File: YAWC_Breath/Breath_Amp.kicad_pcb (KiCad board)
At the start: 2 copper layers, 41 x 32 mm, 20 parts, among them P1 J_IO, P2 PressSens, U1 MCP6002, U2 MPX12DP

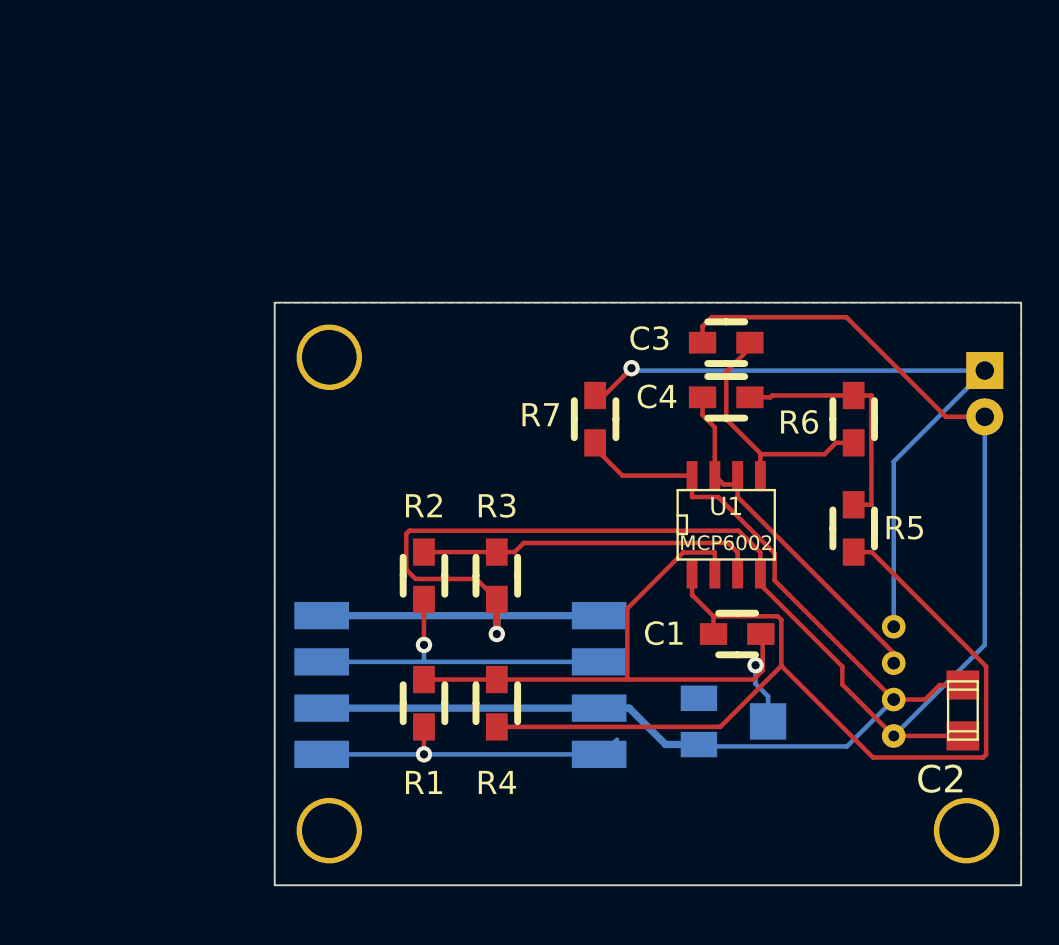
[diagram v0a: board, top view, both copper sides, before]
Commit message: Positioned connector and unrouted old
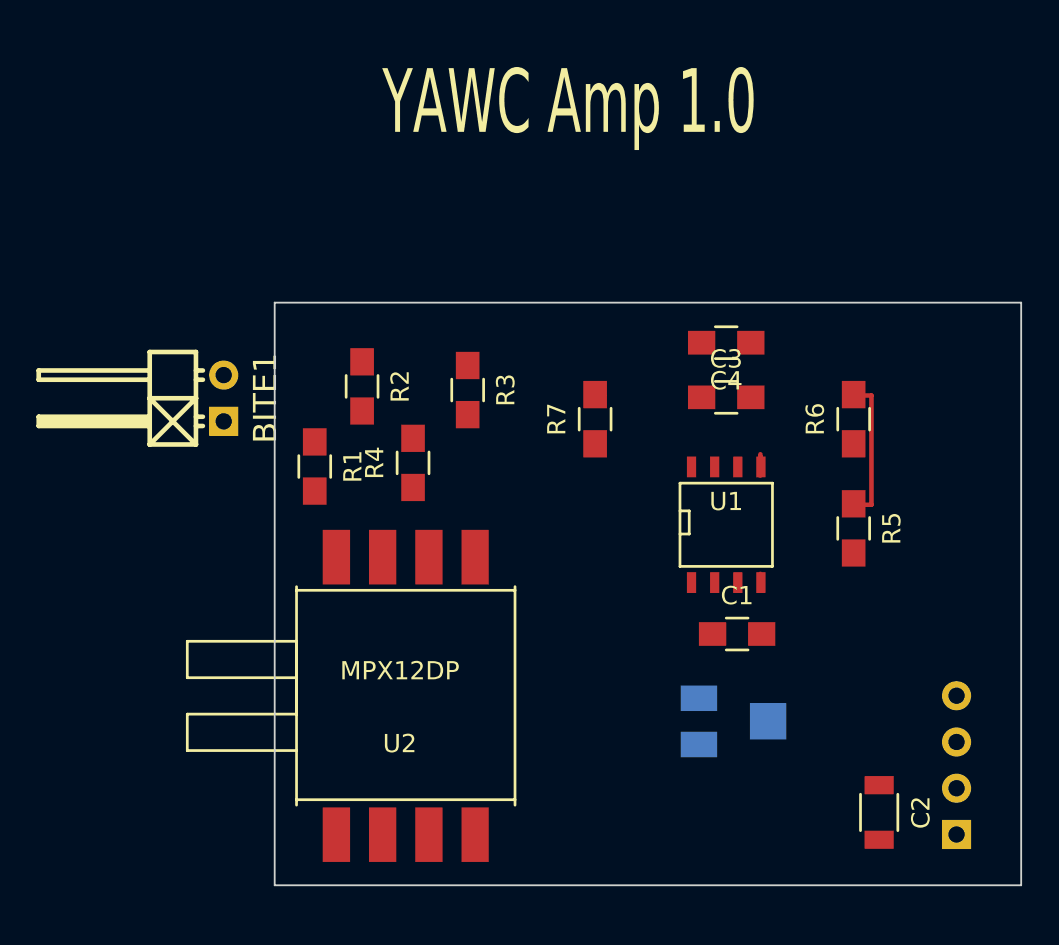
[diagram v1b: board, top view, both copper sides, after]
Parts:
- removed ?: , Wire_Pads:SolderWirePad_single_1-2mmDrill
- removed ? (x3): Hole, Mount:Hole3
- removed P2: PressSens, Pin_Headers:Pin_Header_Angled_1x02
- added BITE1: CONN_01X02, PIN_Hdr:Pin_Header_Angled_1x02, F.Cu at (141.0, 115.2)
- C1, C3, C4, R1, R2, R3, R4, R5, R6, R7: footprint Resistors_SMD:Resistor_SMD0805_HandSoldering -> Resistors_SMD:R_0805_HandSoldering
- C2: footprint Capacitors_SMD:c_1206 -> Capacitors_SMD:C_1206
- P1: footprint JST:JST-4-PH-RA -> PIN_Hdr:Pin_Header_Angled_1x04
- U1: footprint SOIC_Packages:SOIC-8_N -> SMD_Packages:SOIC-8-N
- U2: moved to F.Cu
- moved R1 14.3 mm to (146.0, 119.0)
- moved R4 14.0 mm to (151.4, 118.8)
- moved R2 10.9 mm to (148.6, 114.6)
- moved R3 10.3 mm to (154.4, 114.8)
- moved C2 7.25 mm to (177.0, 138.0), turned to 270 degrees
- moved P1 5.75 mm to (181.2, 135.4)
- moved U2 3.06 mm to (151.0, 131.6), turned to 0 degrees
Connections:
- net VCC renamed /VCC
- RV1 pad 3: Net-(RV1-Pad3) -> GND
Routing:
- net GND: track 101.2 -> 0.59 mm, vias 1 -> 0
- net /VCC: track 62.4 -> 0.30 mm
- net Net-(C1-Pad1): track 55.3 -> 0.00 mm
- net /Pout: track 38.2 -> 0.50 mm, vias 1 -> 0
- net Net-(C1-Pad2): track 35.9 -> 0.14 mm, vias 1 -> 0
- net /Bout: track 19.9 -> 0.00 mm
- net Net-(R2-Pad1): track 18.8 -> 0.00 mm
- net Net-(R2-Pad2): track 18.7 -> 0.00 mm, vias 1 -> 0
- net Net-(R1-Pad2): track 18.1 -> 0.00 mm, vias 1 -> 0
- net Net-(C4-Pad1): track 14.1 -> 1.47 mm
- net Net-(C3-Pad2): track 13.7 -> 7.95 mm
- removed copper zone on B.Cu, net GND
- removed copper zone on F.Cu, net GND

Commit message: Routed. DRC'd. Not gerber viewed
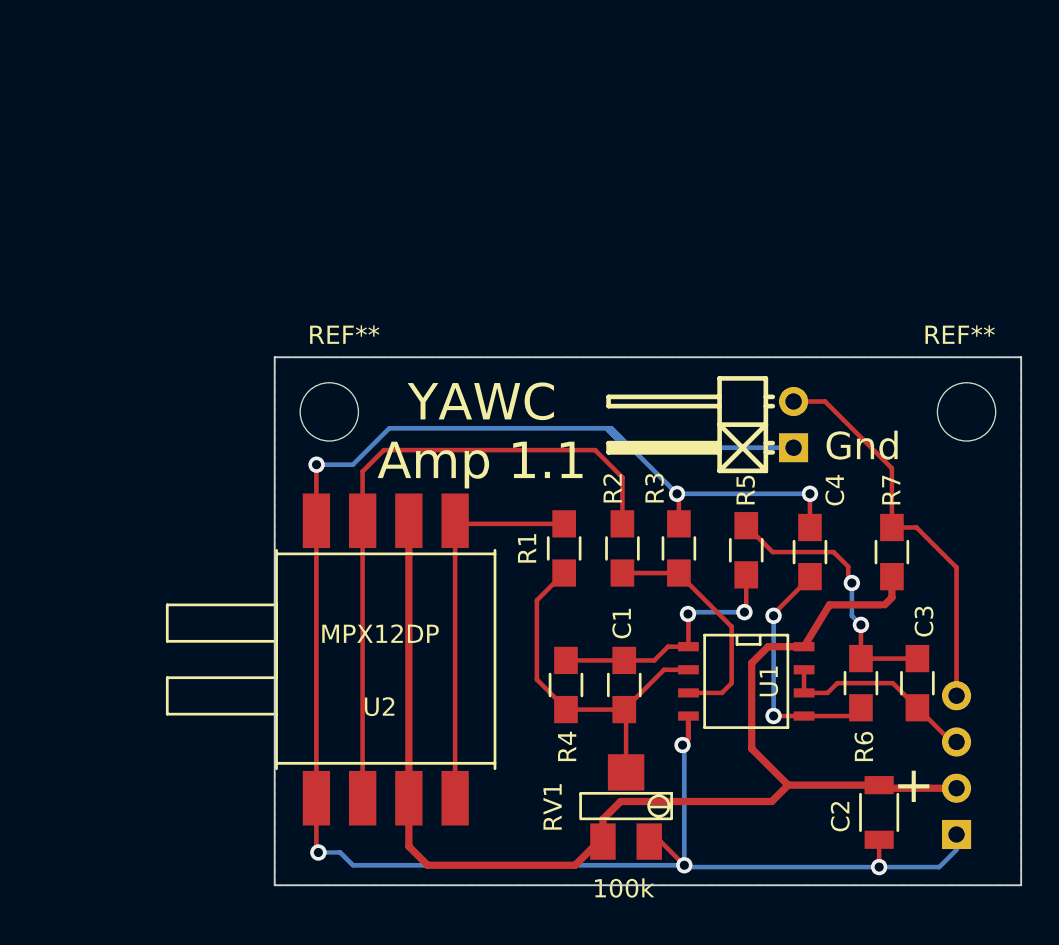
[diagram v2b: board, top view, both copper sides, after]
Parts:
- added REF**: MountingHole_3.2mm_M3, Mounting_Holes:MountingHole_3.2mm_M3, F.Cu at (181.4, 116.0)
- added REF**: MountingHole_3.2mm_M3, Mounting_Holes:MountingHole_3.2mm_M3, F.Cu at (147.6, 116.0)
- RV1: moved to F.Cu
- moved BITE1 31.3 mm to (172.3, 116.7)
- moved C3 18.9 mm to (179.1, 130.9), turned to 90 degrees
- moved R7 17.9 mm to (177.7, 123.7)
- moved R2 16.8 mm to (162.9, 123.5), turned to 90 degrees
- moved R4 14.8 mm to (159.8, 131.0), turned to 270 degrees
- moved R6 14.5 mm to (176.0, 130.9)
- moved R3 14.5 mm to (166.0, 123.5), turned to 90 degrees
- moved R1 14.4 mm to (159.7, 123.5), turned to 90 degrees
- moved C4 12.4 mm to (173.2, 123.7), turned to 90 degrees
- moved U1 8.67 mm to (169.7, 130.8), turned to 270 degrees
- moved RV1 7.54 mm to (163.1, 137.7), turned to 0 degrees
- moved C1 6.80 mm to (163.0, 131.0), turned to 270 degrees
- moved R5 6.02 mm to (169.7, 123.6)
- moved U2 2.28 mm to (149.9, 129.6)
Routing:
- net GND: track 0.59 -> 115.7 mm, vias 0 -> 7
- net /VCC: track 0.30 -> 69.2 mm
- net Net-(R2-Pad2): track 0.00 -> 35.9 mm
- net Net-(R1-Pad2): track 0.00 -> 21.3 mm
- net /Pout: track 0.50 -> 21.7 mm
- net Net-(C1-Pad2): track 0.14 -> 19.9 mm
- net Net-(C1-Pad1): track 0.00 -> 14.1 mm, vias 0 -> 2
- net Net-(R2-Pad1): track 0.00 -> 12.9 mm
- net Net-(C4-Pad1): track 1.47 -> 13.5 mm, vias 0 -> 2
- net /Bout: track 0.00 -> 11.2 mm
- net Net-(C3-Pad2): track 7.95 -> 15.0 mm, vias 0 -> 2
- added copper zone on B.Cu, net GND
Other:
- board size 41 x 32 mm -> 41 x 29 mm
- board text added: "+"
- board text added: "Gnd"
- board text added: "YAWC Amp 1.1"
- board text removed: "YAWC Amp 1.0"
